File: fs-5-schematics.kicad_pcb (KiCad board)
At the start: 2 copper layers, 34 x 36.8 mm, 13 parts, among them J1 12V, J2 5V, U1 TPS54202DDC

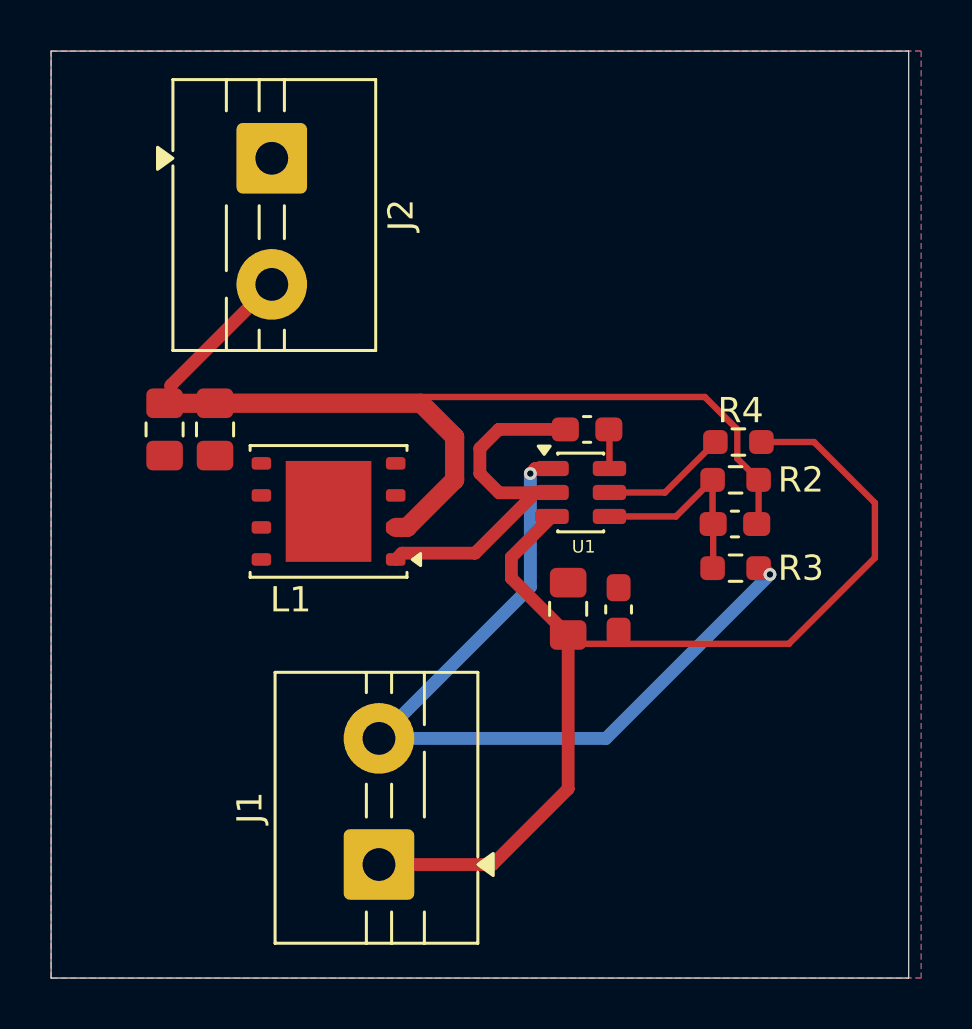
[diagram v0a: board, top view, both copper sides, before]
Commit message: cleaned up formatting, found Inductor footprint, layouts finished
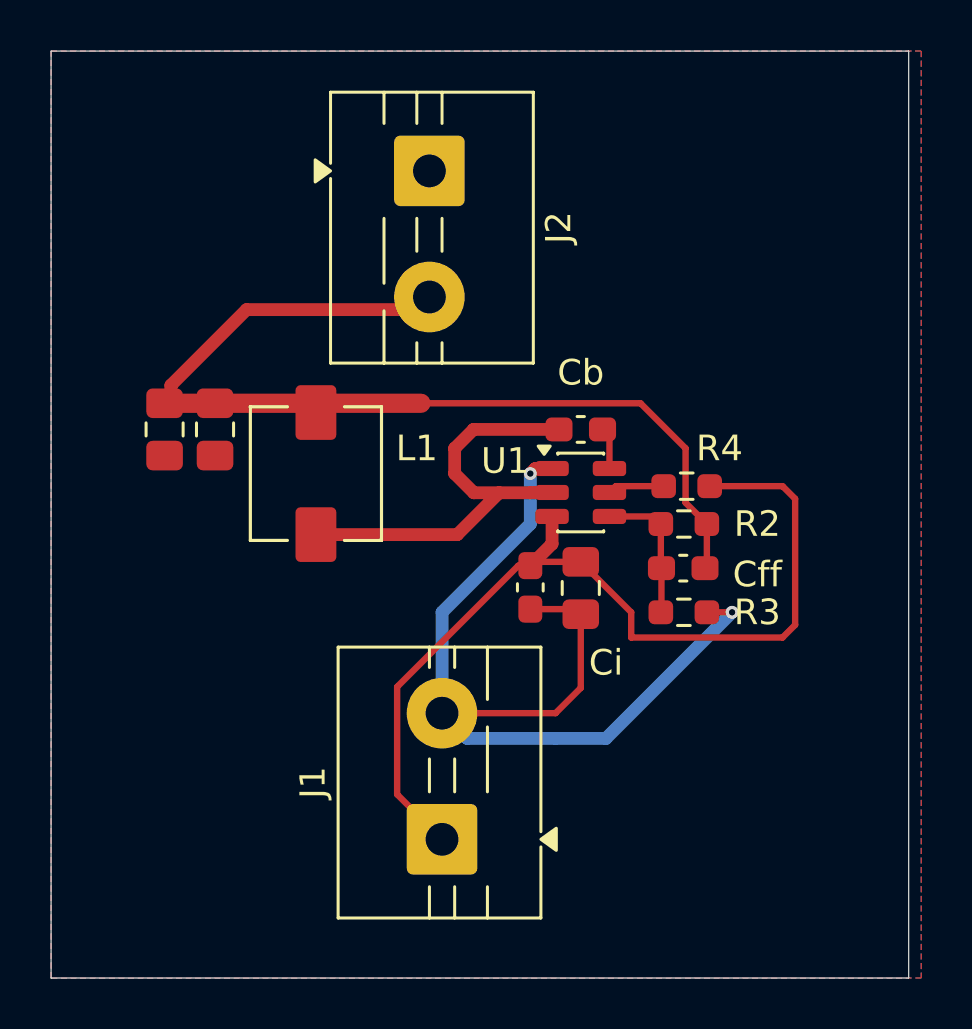
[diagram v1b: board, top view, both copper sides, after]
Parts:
- L1: value 10uH -> INDM5752X300N; footprint Package_SON:WSON-8-1EP_6x5mm_P1.27mm_EP3.4x4mm -> Project_parts:INDM5752X300N
- moved J2 6.27 mm to (84.0, 39.5)
- moved Cdecoupling1 3.61 mm to (88.0, 56.0), turned to -90 degrees
- moved Cfeedfoward1 2.70 mm to (94.1, 55.2)
- moved R2 2.70 mm to (94.1, 53.5)
- moved R3 2.70 mm to (94.1, 57.0)
- moved R4 2.70 mm to (94.2, 52.0)
- moved J1 2.69 mm to (84.5, 66.0)
- moved L1 1.58 mm to (79.5, 51.5), turned to -90 degrees
- moved Ci 0.96 mm to (90.0, 56.0), turned to -90 degrees
- moved Cb 0.25 mm to (90.0, 49.8)
- renumbered Cboost1 to Cb, Cinput1 to Ci
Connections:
- L1 pad 1: Net-(U1-SW) -> +5V
- L1 pad 2: +5V -> Net-(U1-SW)
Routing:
- net +5V: track 48.8 -> 39.4 mm
- net GND: track 32.7 -> 37.9 mm
- net +12V: track 42.5 -> 39.0 mm
- net Net-(U1-EN): track 5.44 -> 2.67 mm
- net Net-(U1-SW): track 15.2 -> 17.6 mm
- net Net-(U1-FB): track 8.35 -> 6.01 mm
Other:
- board text added: "Cff"
